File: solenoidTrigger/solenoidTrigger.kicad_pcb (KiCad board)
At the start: 2 copper layers, 88.9 x 88.9 mm, 42 parts, among them J8 CONN_02X03, P1 OSTTC03, P2 OSTTC02, P3 OSTTC08, P4 OSTTC03, P5 OSTTC03, Q1 NMOS_CDS16, Q2 NMOS_CDS16, Q3 NMOS_CDS16, Q4 NMOS_CDS16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

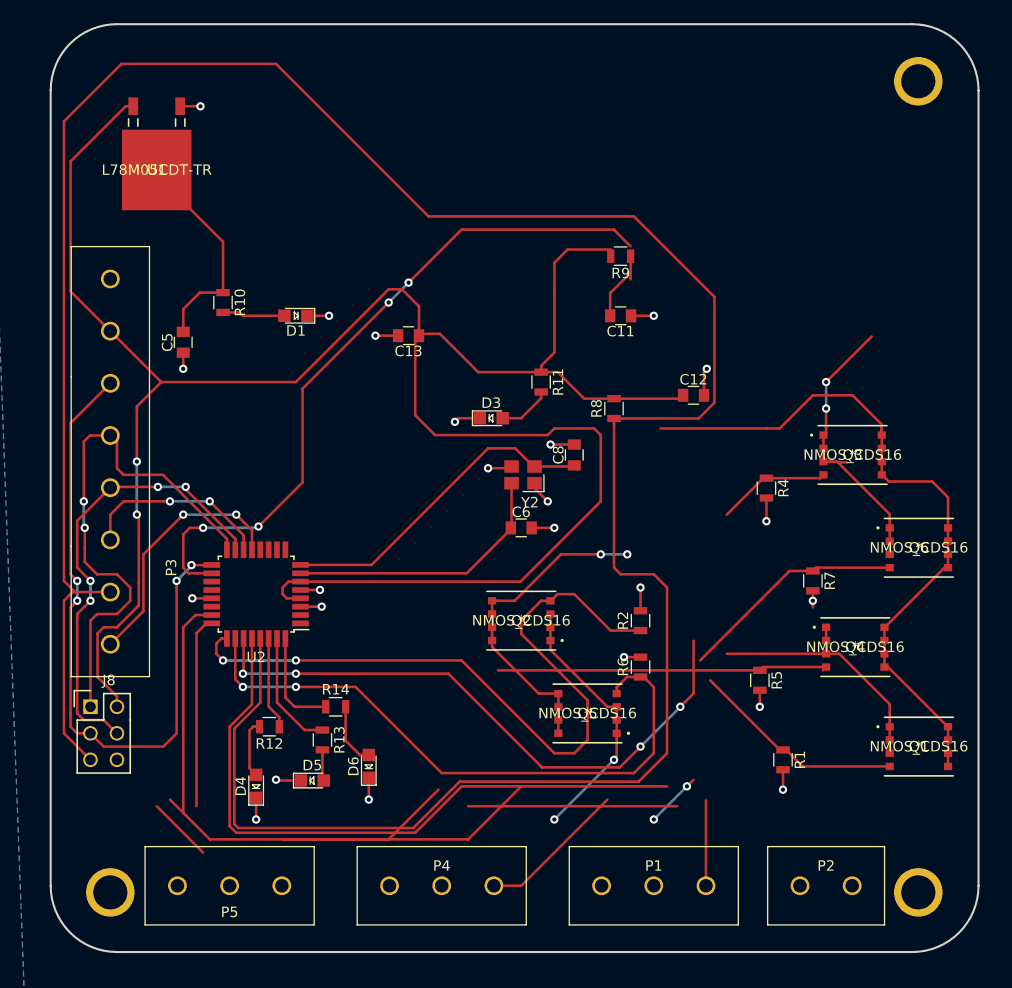
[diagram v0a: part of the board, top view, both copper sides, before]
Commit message: moved 3 pin connector
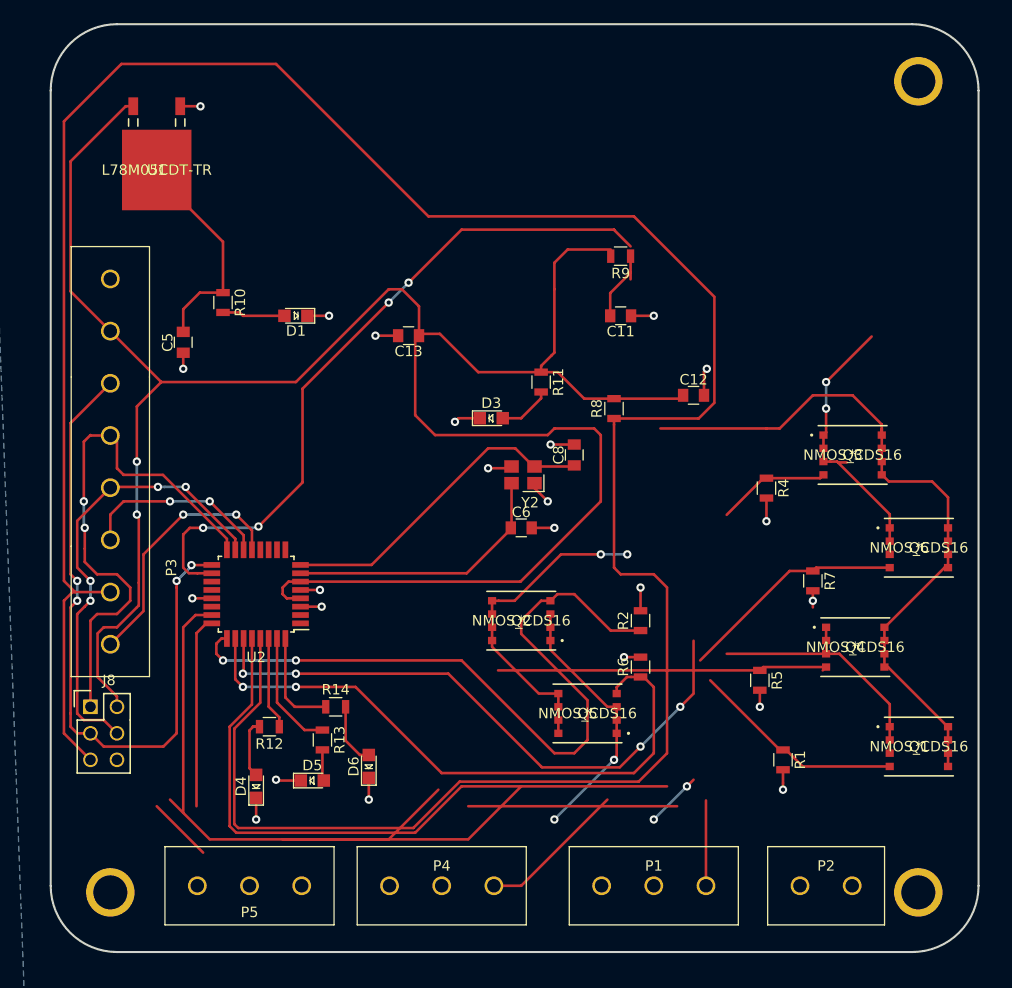
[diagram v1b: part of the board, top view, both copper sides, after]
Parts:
- moved P5 1.91 mm to (121.9, 132.1)

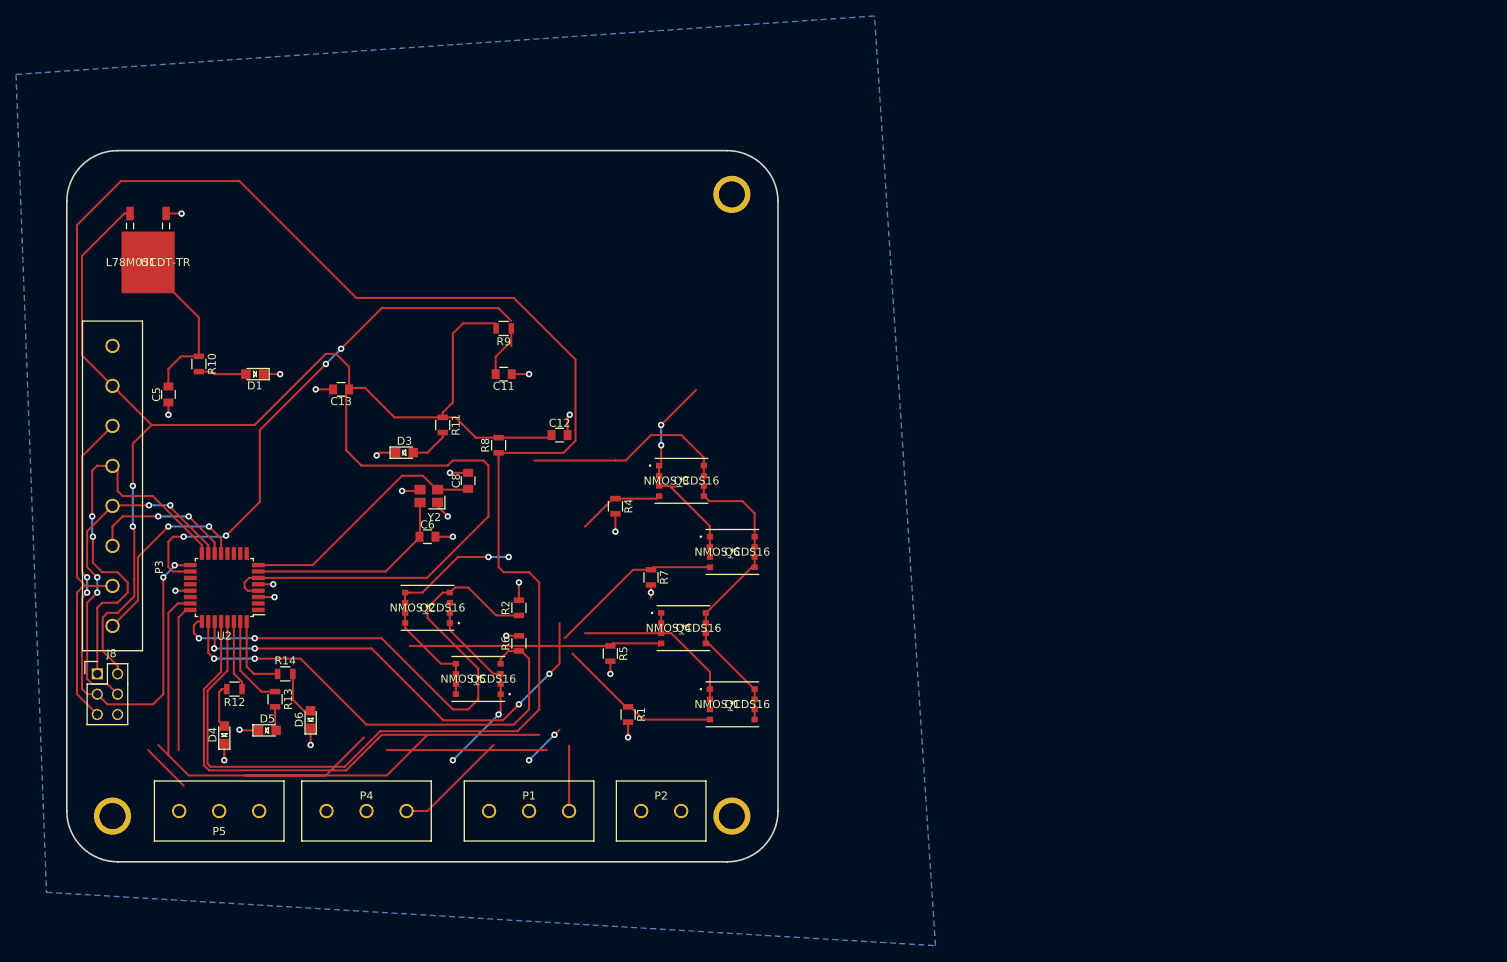
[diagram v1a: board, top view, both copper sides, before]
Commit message: Created part for fuse reciprocal, deleted most traces, laying out board again to improve organization and performance
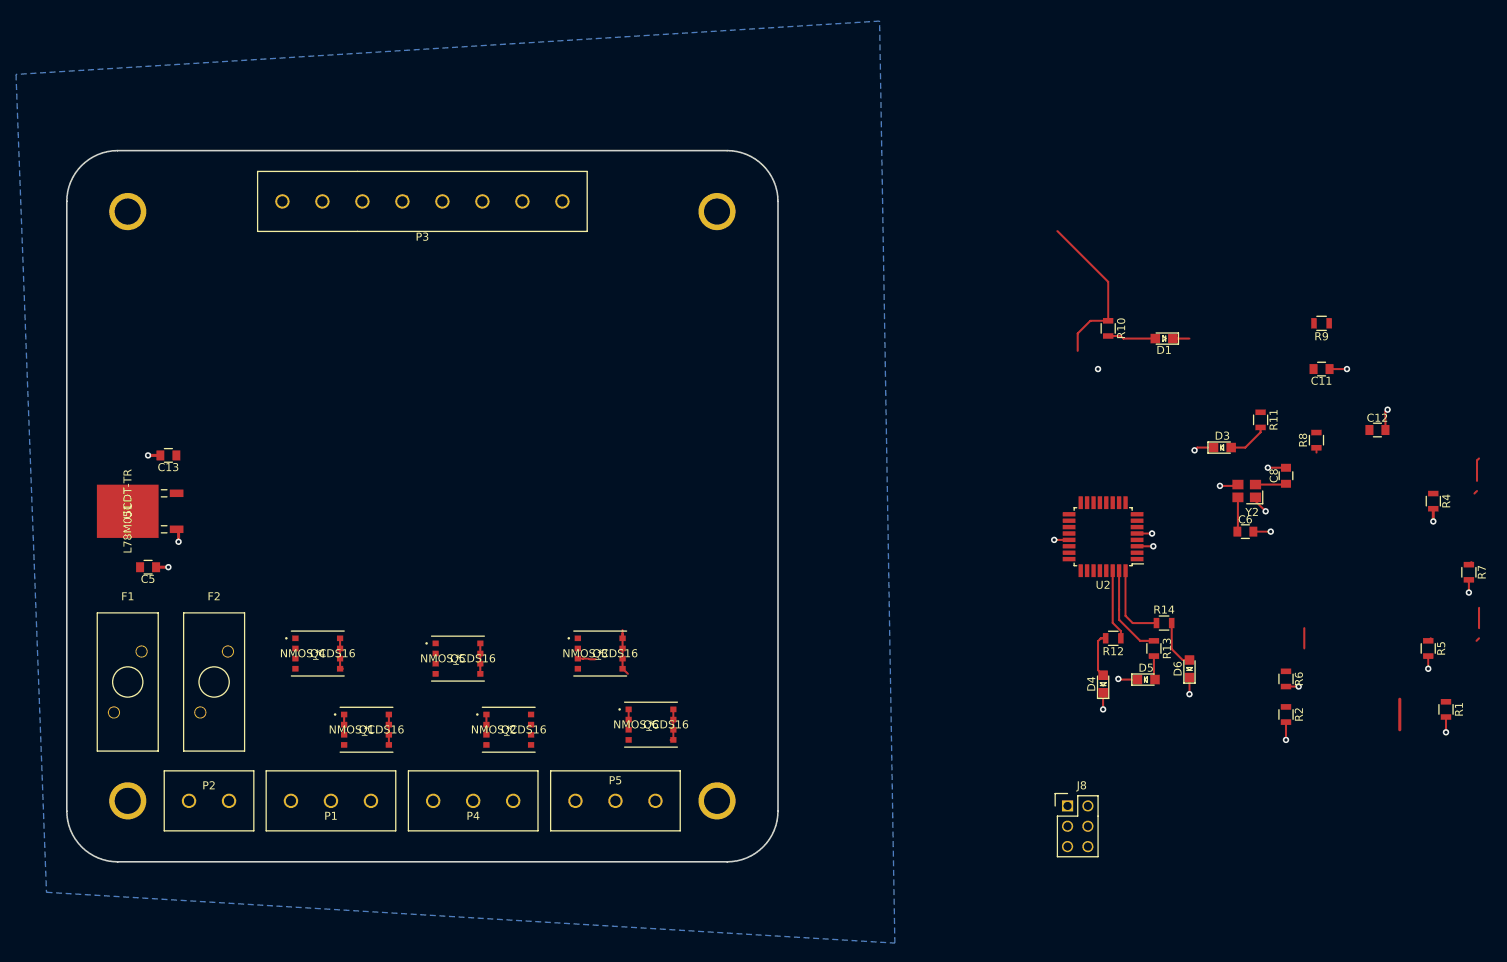
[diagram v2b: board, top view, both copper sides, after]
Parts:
- removed the REF** at (108.6, 132.7)
- removed the REF** at (186.0, 132.7)
- removed the REF** at (186.0, 55.0)
- added F1: 01530008Z, footprints:01530008Z, F.Cu at (110.5, 104.8)
- added F2: 01530008Z, footprints:01530008Z, F.Cu at (121.3, 104.8)
- added REF**: Mounting_Hole_4-40, footprints:Mounting_Hole_4-40, F.Cu at (110.5, 57.1)
- added REF**: Mounting_Hole_4-40, footprints:Mounting_Hole_4-40, F.Cu at (184.2, 130.8)
- added REF**: Mounting_Hole_4-40, footprints:Mounting_Hole_4-40, F.Cu at (110.5, 130.8)
- added REF**: Mounting_Hole_4-40, footprints:Mounting_Hole_4-40, F.Cu at (184.2, 57.1)
- moved J8 122.4 mm to (228.0, 131.4)
- moved D1 113.8 mm to (240.0, 73.0)
- moved R10 113.8 mm to (233.0, 71.8)
- moved D6 110.0 mm to (243.2, 114.3)
- moved R12 110.0 mm to (233.7, 110.5)
- moved D4 110.0 mm to (232.4, 116.2)
- moved D5 110.0 mm to (237.8, 115.7)
- moved R13 110.0 mm to (238.8, 111.8)
- moved R14 110.0 mm to (240.0, 108.6)
- moved U2 110.0 mm to (232.4, 97.8)
- moved C8 102.2 mm to (255.3, 90.2)
- moved R4 102.2 mm to (273.7, 93.3)
- moved R5 102.2 mm to (273.1, 111.8)
- moved Y2 102.2 mm to (250.4, 92.1)
- moved C11 102.2 mm to (259.7, 76.8)
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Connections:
- P2 pad 1: (no net) -> Net-(F1-Pad2)
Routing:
- net /RESET: track 260.3 -> 0.60 mm
- net VCC: track 215.0 -> 0.88 mm, vias 2 -> 0
- net /ctrl_pin_1-2: track 104.7 -> 1.43 mm
- net /ctrl_pin_3-2: track 84.7 -> 0.45 mm
- net Net-(C11-Pad2): track 74.5 -> 0.30 mm, vias 4 -> 0
- net /12V_Switch: track 98.9 -> 26.2 mm, vias 2 -> 0
- net /ctrl_pin_2-1: track 70.2 -> 0.04 mm, vias 2 -> 0
- net /ctrl_pin_3-1: track 69.1 -> 0.75 mm, vias 4 -> 0
- net /SCK: track 65.1 -> 0.02 mm, vias 4 -> 0
- net /ctrl_pin_2-2: track 59.8 -> 0.30 mm, vias 2 -> 0
- net /12V_Solenoid2: track 59.6 -> 5.08 mm, vias 2 -> 0
- net /MISO: track 52.3 -> 1.41 mm, vias 2 -> 0
- net /ctrl_pin_1-1: track 47.9 -> 0.60 mm
- net /MOSI: track 43.9 -> 0.10 mm, vias 4 -> 0
- net /12V_Solenoid1: track 38.5 -> 5.08 mm, vias 2 -> 0
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
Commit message: Continued laying out components on board
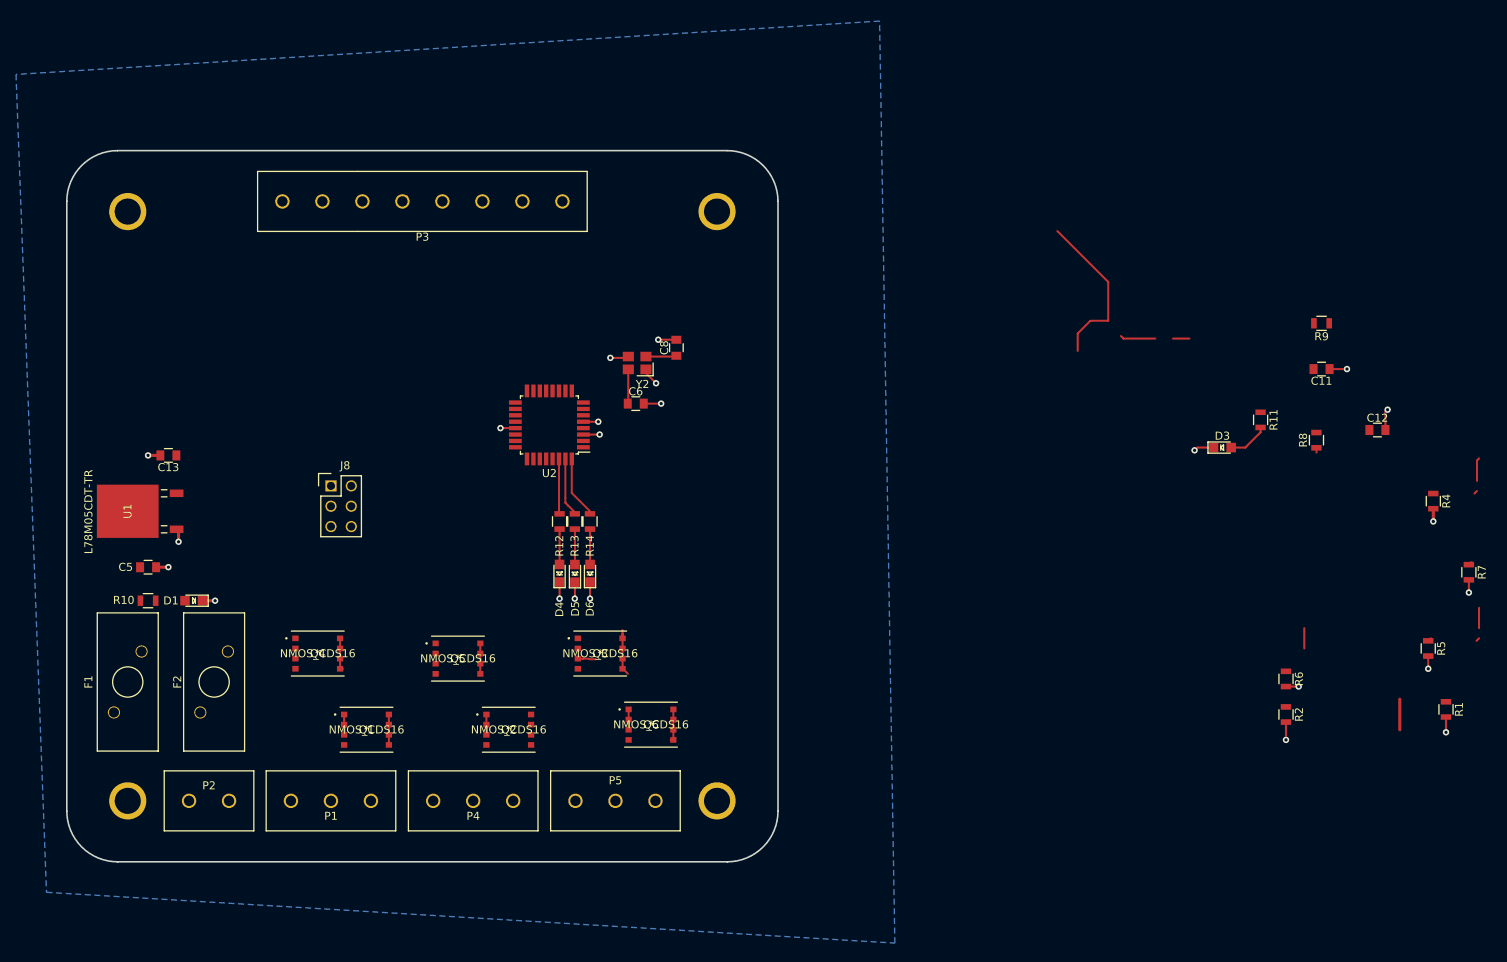
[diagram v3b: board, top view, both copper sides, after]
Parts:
- moved D1 125.6 mm to (118.7, 105.8)
- moved R10 124.7 mm to (113.0, 105.8), turned to 0 degrees
- moved J8 100.4 mm to (135.9, 91.4)
- moved C8 77.9 mm to (179.1, 74.2)
- moved Y2 77.9 mm to (174.2, 76.1)
- moved C6 77.9 mm to (174.0, 81.2)
- moved D6 75.9 mm to (168.3, 102.4)
- moved R13 74.1 mm to (166.4, 95.9)
- moved R14 72.9 mm to (168.3, 95.9), turned to 270 degrees
- moved D5 72.6 mm to (166.4, 102.4), turned to 90 degrees
- moved R12 70.7 mm to (164.5, 95.9), turned to 270 degrees
- moved U2 70.6 mm to (163.2, 83.8)
- moved D4 69.3 mm to (164.5, 102.4)
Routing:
- net /PLED2: track 11.7 -> 7.07 mm
- net /PLED3: track 10.4 -> 8.01 mm
- net /PLED1: track 8.87 -> 6.53 mm
- net Net-(D4-Pad2): track 6.23 -> 4.43 mm
- net Net-(D5-Pad2): track 2.99 -> 4.79 mm
- net Net-(D6-Pad2): track 6.04 -> 4.43 mm
- net Net-(D1-Pad2): track 6.02 -> 4.43 mm
- net GND: track 46.1 -> 47.4 mm

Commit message: continued moving around components
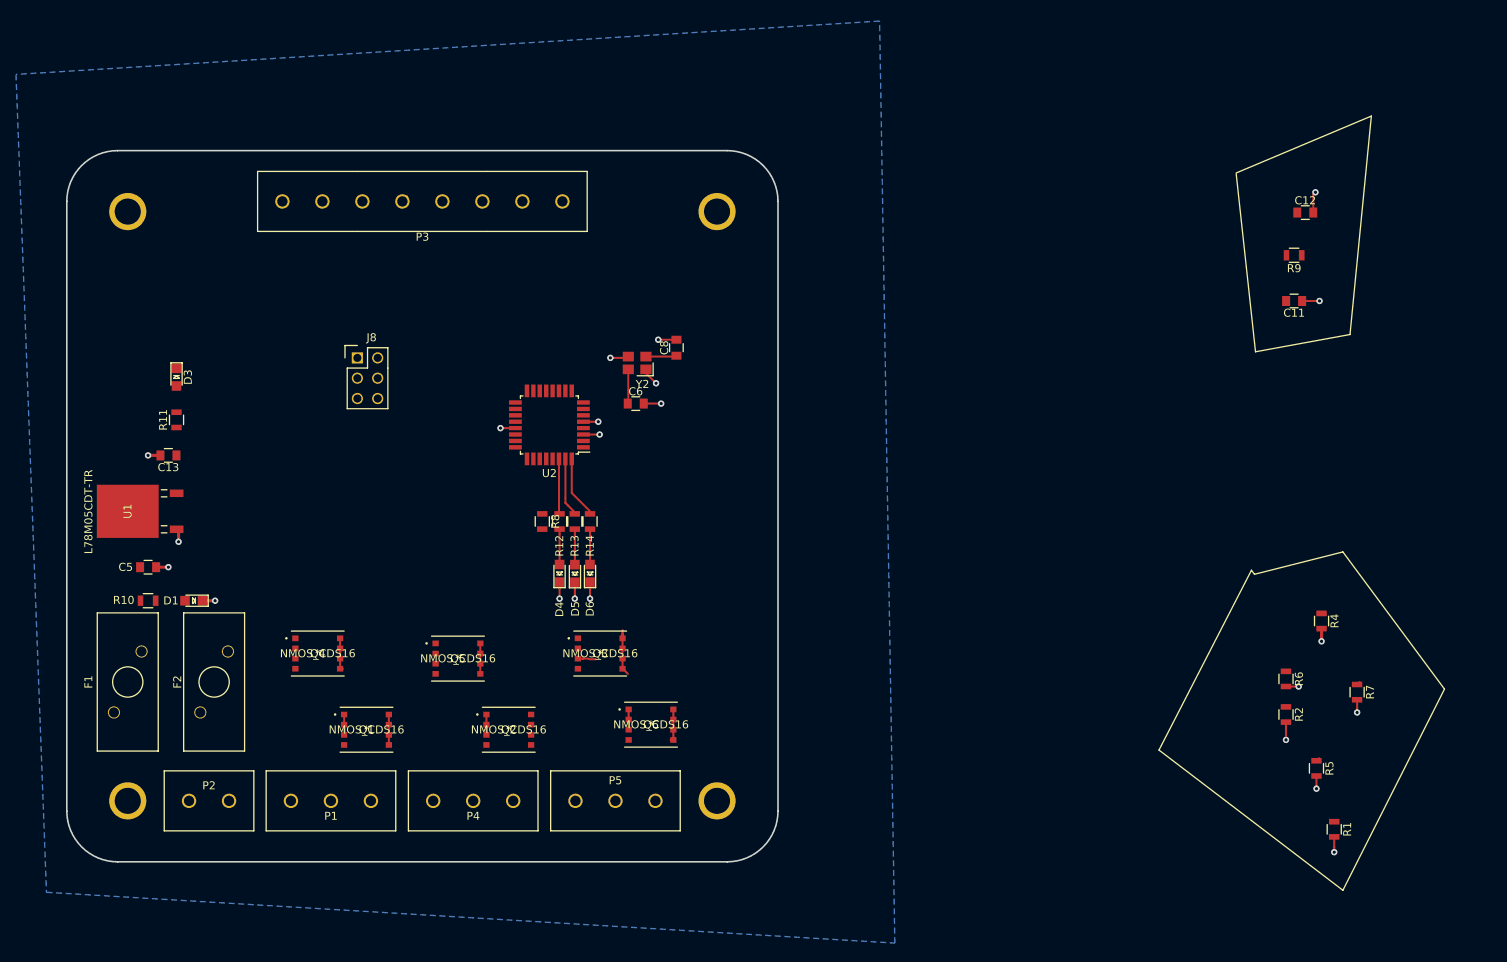
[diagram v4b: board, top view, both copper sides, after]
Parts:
- moved R11 135.5 mm to (116.6, 83.2), turned to 90 degrees
- moved D3 131.0 mm to (116.6, 77.9), turned to 270 degrees
- moved R8 97.3 mm to (162.3, 95.9), turned to 270 degrees
- moved C12 28.6 mm to (257.7, 57.3)
- moved R4 20.5 mm to (259.7, 108.3)
- moved R5 20.5 mm to (259.1, 126.7)
- moved R1 20.5 mm to (261.3, 134.4)
- moved R7 20.5 mm to (264.2, 117.2)
- moved J8 16.3 mm to (139.2, 75.4)
- moved R9 9.17 mm to (256.3, 62.6)
- moved C11 9.17 mm to (256.3, 68.3)
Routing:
- net /12V: track 20.5 -> 0.00 mm
- net Net-(D3-Pad2): track 5.07 -> 0.00 mm
- net GND: track 47.4 -> 42.8 mm, vias 23 -> 22
- net Net-(D1-Pad2): track 4.43 -> 0.00 mm
- net /12V_Switch: track 26.2 -> 22.4 mm
- net /12V_Solenoid3: track 7.54 -> 4.64 mm
- net /12V_Solenoid2: track 5.08 -> 2.54 mm
- net /12V_Solenoid1: track 5.08 -> 2.54 mm
- net /RESET: track 0.60 -> 0.00 mm
